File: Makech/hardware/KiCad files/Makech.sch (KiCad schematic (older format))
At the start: 45 parts, among them IC1 ULN2803, J1 USB_B_Micro, J2 SWD programmer, J3 ESP32-Exp, SW1 RST, U1 CONN_01X04, U2 ATSAMD21G18A-AU, U6 AP2114_3.3v, X1 Screw_Terminal_1x02

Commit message: Footprint complet
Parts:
- removed C2.1: 100nF, Capacitor_SMD:C_0603_1608Metric_Pad1.05x0.95mm_HandSolder, symbol Makech-rescue:C-RESCUE-Ogaki--Ogaki-rescue-Makech-rescue-Makech-rescue-Makech-r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
- removed R1, R3: 10K, Resistor_SMD:R_Array_Concave_2x0603, symbol Makech-rescue:R-SIL_8NB--Ogaki-rescue-Makech-rescue-Makech-rescue-Makech-rescue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
- removed R2: 10K, Resistors_SMD:R_0805_HandSoldering, symbol Makech-rescue:R-SIL_8NB--Ogaki-rescue-Makech-rescue-Makech-rescue-Makech-rescue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
- removed R4, R5: 1K, Resistors_ThroughHole:R_Array_SIP4, symbol Makech-rescue:R-SIL_8NB--Ogaki-rescue-Makech-rescue-Makech-rescue-Makech-rescue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
- removed S1, S2, S4, S5: switch, Button_Switch_THT:SW_PUSH-12mm_Wuerth-430476085716, symbol Makech-rescue:switch--Ogaki-rescue-Makech-rescue-Makech-rescue-Makech-rescue-Ma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
- removed S3: switch, Button_Switch_THT:SW_PUSH-12mm, symbol Makech-rescue:switch--Ogaki-rescue-Makech-rescue-Makech-rescue-Makech-rescue-Ma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
- removed S7: switch, Button_Switch_THT:SW_CuK_OS102011MA1QN1_SPDT_Angled, symbol Makech-rescue:switch--Ogaki-rescue-Makech-rescue-Makech-rescue-Makech-rescue-Ma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
- added R1, R2, R3, R4, R5, R6: 10K, Resistor_SMD:R_0805_2012Metric_Pad1.15x1.40mm_HandSolder, symbol Device:R_Small
- added R10, R11, R12, R9: 1K, Resistor_SMD:R_0805_2012Metric_Pad1.15x1.40mm_HandSolder, symbol Device:R_Small
- added S1, S2, S3, S4, S5: switch, Button_Switch_THT:SW_PUSH-12mm_Wuerth-430476085716, symbol Makech-rescue:SW_Push-Switch-Makech-rescue-Makech-rescue-Makech-rescue-Makech-r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
- added SW2: SW_DPDT_x2, Button_Switch_THT:SW_CuK_OS102011MA1QN1_SPDT_Angled, symbol Switch:SW_DPDT_x2
- SJ1: renamed from SJ2; footprint Connect:GS2 -> Jumper:SolderJumper-2_P1.3mm_Open_TrianglePad1.0x1.5mm
- X1: footprint Connect:bornier2 -> TerminalBlock:TerminalBlock_Altech_AK300-2_P5.00mm
- XH2: renamed from XH4; footprint Connector_Molex:Molex_KK-254_AE-6410-04A_1x04_P2.54mm_Vertical -> Connector_Molex:Molex_KK-254_AE-6410-05A_1x05_P2.54mm_Vertical
- renumbered C5 to C2, C6 to C3, C3 to C4, C4 to C5, C2 to C6, J2 to J1, J1 to J2, R6 to R7, R7 to R8, U2 to U1, U1 to U2, U6 to U3, XH3 to XH1
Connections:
- wire segments 280 -> 239
- no-connect marks 9 -> 10
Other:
- note removed: "Blue"

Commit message: Complete
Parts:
- J1: footprint Connector_PinHeader_1.00mm:PinHeader_2x02_P1.00mm_Vertical_SMD -> Connector_PinHeader_2.54mm:PinHeader_2x02_P2.54mm_Vertical_SMD
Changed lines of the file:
@@
 Text Label 7645 2390 0    60   ~ 0
 A3
-Text Label 5755 1260 1    60   ~ 0
-S1
-Text Label 6180 1260 1    60   ~ 0
-S2
-Text Label 6645 1260 1    60   ~ 0
-S3
-Text Label 7110 1255 1    60   ~ 0
-S5
-Text Label 7570 1270 1    60   ~ 0
-S4
 $Comp
 L Makech-rescue:JUMPER--Ogaki-rescue-Makech-rescue-Makech-rescue-Makech-rescue-Makech-rescue-Makech-rescue-Makech-rescue-Makech-rescue-Makech-rescue SJ1
@@
 F 0 "J1" H 1305 5897 50  0000 C CNN
 F 1 "SWD programmer" H 1305 5806 50  0000 C CNN
-F 2 "Connector_PinHeader_1.00mm:PinHeader_2x02_P1.00mm_Vertical_SMD" H 1255 5680 50  0001 C CNN
+F 2 "Connector_PinHeader_2.54mm:PinHeader_2x02_P2.54mm_Vertical_SMD" H 1255 5680 50  0001 C CNN
 F 3 "~" H 1255 5680 50  0001 C CNN
 	1    1255 5680

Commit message: USB correct
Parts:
- J2: footprint Connector_USB:USB_Micro-B_Amphenol_10103594-0001LF_Horizontal -> Connector_USB:USB_Micro-B_Wuerth_629105150521
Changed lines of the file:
@@
 F 0 "J2" H 2705 6257 50  0000 C CNN
 F 1 "USB_B_Micro" H 2705 6166 50  0000 C CNN
-F 2 "Connector_USB:USB_Micro-B_Amphenol_10103594-0001LF_Horizontal" H 2800 5740 50  0001 C CNN
+F 2 "Connector_USB:USB_Micro-B_Wuerth_629105150521" H 2800 5740 50  0001 C CNN
 F 3 "~" H 2800 5740 50  0001 C CNN
 F 4 "629105150521" H 2650 5790 50  0001 C CNN "manf#"

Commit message: change leds 3mm
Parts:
- J1: footprint Connector_PinHeader_2.54mm:PinHeader_2x02_P2.54mm_Vertical_SMD -> Pines:621X0421021
- LED1, LED2, LED3, LED4: footprint LED_SMD:LED_0805_2012Metric -> LEDs:LED_D3.0mm
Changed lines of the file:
@@
 F 0 "LED1" H 5755 3060 40  0000 C CNN
 F 1 "L" H 5755 2860 40  0001 C CNN
-F 2 "LED_SMD:LED_0805_2012Metric" H 5755 2960 60  0001 C CNN
+F 2 "LEDs:LED_D3.0mm" H 5755 2960 60  0001 C CNN
 F 3 "" H 5755 2960 60  0000 C CNN
 F 4 "APT2012LVBC/D" H 5755 2960 50  0001 C CNN "manf#"
@@
 F 0 "LED2" H 6385 3060 40  0000 C CNN
 F 1 "L" H 6385 2860 40  0001 C CNN
-F 2 "LED_SMD:LED_0805_2012Metric" H 6385 2960 60  0001 C CNN
+F 2 "LEDs:LED_D3.0mm" H 6385 2960 60  0001 C CNN
 F 3 "" H 6385 2960 60  0000 C CNN
 F 4 "APT2012SRCPRV" H 6385 2960 50  0001 C CNN "manf#"
@@
 F 0 "LED3" H 7015 3060 40  0000 C CNN
 F 1 "L" H 7015 2860 40  0001 C CNN
-F 2 "LED_SMD:LED_0805_2012Metric" H 7015 2960 60  0001 C CNN
+F 2 "LEDs:LED_D3.0mm" H 7015 2960 60  0001 C CNN
 F 3 "" H 7015 2960 60  0000 C CNN
 F 4 "APT2012SECK" H 7015 2960 50  0001 C CNN "manf#"
@@
 F 0 "LED4" H 7645 3060 40  0000 C CNN
 F 1 "L" H 7645 2860 40  0001 C CNN
-F 2 "LED_SMD:LED_0805_2012Metric" H 7645 2960 60  0001 C CNN
+F 2 "LEDs:LED_D3.0mm" H 7645 2960 60  0001 C CNN
 F 3 "" H 7645 2960 60  0000 C CNN
 F 4 "APT2012SGC" H 7645 2960 50  0001 C CNN "manf#"
@@
 F 0 "J1" H 1305 5897 50  0000 C CNN
 F 1 "SWD programmer" H 1305 5806 50  0000 C CNN
-F 2 "Connector_PinHeader_2.54mm:PinHeader_2x02_P2.54mm_Vertical_SMD" H 1255 5680 50  0001 C CNN
+F 2 "Pines:621X0421021" H 1255 5680 50  0001 C CNN
 F 3 "~" H 1255 5680 50  0001 C CNN
 	1    1255 5680

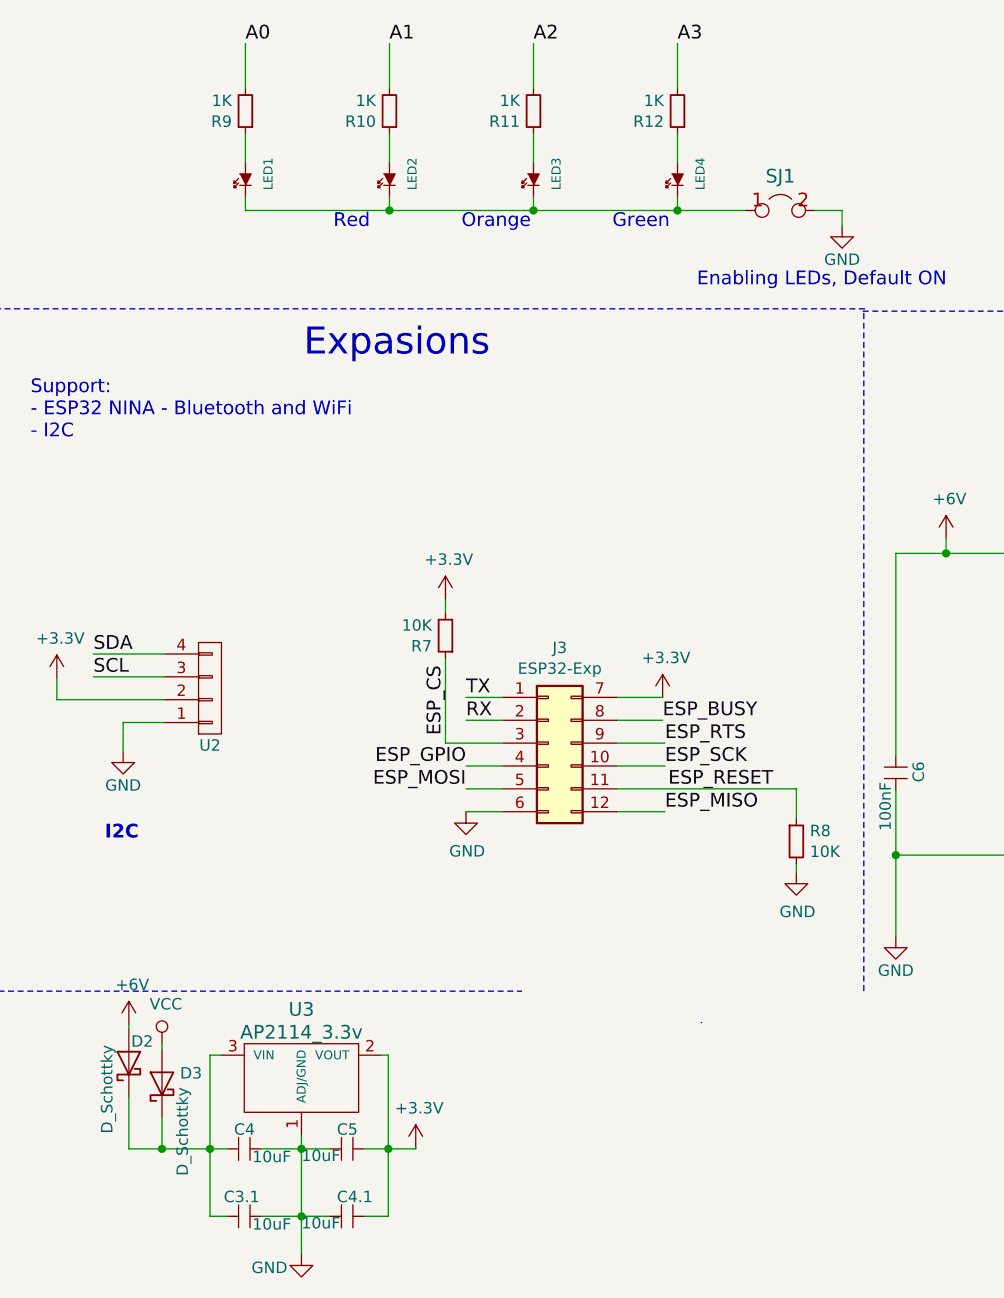
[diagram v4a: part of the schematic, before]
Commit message: remove jumper extra and capacitors
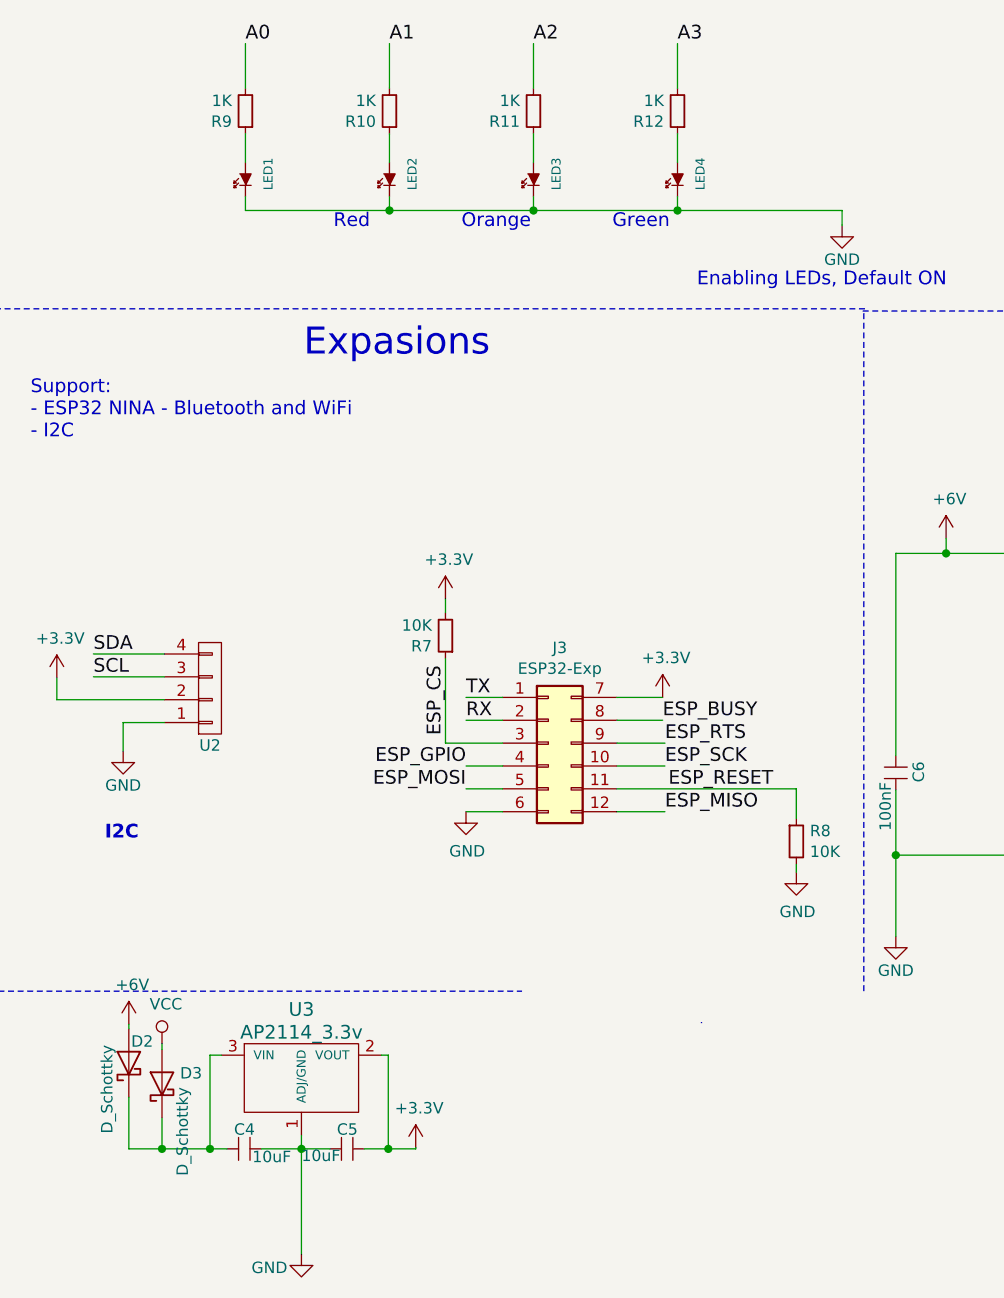
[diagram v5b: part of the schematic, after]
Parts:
- removed C3.1, C4.1: 10uF, Capacitor_SMD:C_0805_2012Metric_Pad1.15x1.40mm_HandSolder, symbol Makech-rescue:C-RESCUE-Ogaki--Ogaki-rescue-Makech-rescue-Makech-rescue-Makech-r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
- removed SJ1: JUMPER, Jumper:SolderJumper-2_P1.3mm_Open_TrianglePad1.0x1.5mm, symbol Makech-rescue:JUMPER--Ogaki-rescue-Makech-rescue-Makech-rescue-Makech-rescue-Ma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
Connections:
- net +3V3: now also C5.1, U3.2 (VOUT)
- net GND: now also LED1.1 (K), LED2.1 (K), LED3.1 (K), LED4.1 (K)
- net at C4.2, U3.3 (VIN): now also D2.1 (K), D3.1 (K)
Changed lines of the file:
@@
 A3
-$Comp
-L Makech-rescue:JUMPER--Ogaki-rescue-Makech-rescue-Makech-rescue-Makech-rescue-Makech-rescue-Makech-rescue-Makech-rescue-Makech-rescue-Makech-rescue SJ1
-U 1 1 58BAD83A
-P 8095 3120
-F 0 "SJ1" H 8095 3270 60  0000 C CNN
-F 1 "JUMPER" H 8095 3040 40  0001 C CNN
-F 2 "Jumper:SolderJumper-2_P1.3mm_Open_TrianglePad1.0x1.5mm" H 8095 3120 60  0001 C CNN
-F 3 "" H 8095 3120 60  0000 C CNN
-	1    8095 3120
-	1    0    0    -1
-$EndComp
 $Comp
 L Makech-rescue:GND--Ogaki-rescue-Makech-rescue-Makech-rescue-Makech-rescue-Makech-rescue-Makech-rescue-Makech-rescue-Makech-rescue-Makech-rescue #PWR026
@@
 	4190 495  4190 3360
 Wire Wire Line
-	8245 3120 8365 3120
-Wire Wire Line
 	8365 3120 8365 3185
 Wire Wire Line
@@
 	5600 6815 5650 6815
 Wire Wire Line
-	5675 7225 5600 7225
-Connection ~ 5600 7225
-Wire Wire Line
 	5825 7225 6000 7225
-Wire Wire Line
-	6275 7225 6380 7225
-Connection ~ 6380 7225
-$Comp
-L Makech-rescue:C-RESCUE-Ogaki--Ogaki-rescue-Makech-rescue-Makech-rescue-Makech-rescue-Makech-rescue-Makech-rescue-Makech-rescue-Makech-rescue-Makech-rescue C3.1
-U 1 1 58DE2448
-P 5775 7520
-F 0 "C3.1" V 5690 7405 50  0000 L CNN
-F 1 "10uF" V 5810 7530 50  0000 L CNN
-F 2 "Capacitor_SMD:C_0805_2012Metric_Pad1.15x1.40mm_HandSolder" H 5775 7520 60  0001 C CNN
-F 3 "" H 5775 7520 60  0000 C CNN
-F 4 "C0805X106K8RACAUTO" V 5775 7520 50  0001 C CNN "manf#"
-	1    5775 7520
-	0    1    1    0
-$EndComp
-$Comp
-L Makech-rescue:C-RESCUE-Ogaki--Ogaki-rescue-Makech-rescue-Makech-rescue-Makech-rescue-Makech-rescue-Makech-rescue-Makech-rescue-Makech-rescue-Makech-rescue C4.1
-U 1 1 58DE26E6
-P 6225 7520
-F 0 "C4.1" V 6140 7450 50  0000 L CNN
-F 1 "10uF" V 6255 7295 50  0000 L CNN
-F 2 "Capacitor_SMD:C_0805_2012Metric_Pad1.15x1.40mm_HandSolder" H 6225 7520 60  0001 C CNN
-F 3 "" H 6225 7520 60  0000 C CNN
-F 4 "C0805X106K8RACAUTO" V 6225 7520 50  0001 C CNN "manf#"
-	1    6225 7520
-	0    1    1    0
-$EndComp
-Wire Wire Line
-	5825 7520 6000 7520
-Wire Wire Line
-	5600 7520 5675 7520
-Wire Wire Line
-	6380 7520 6275 7520
-Wire Wire Line
-	6380 6815 6380 7225
-Wire Wire Line
-	5600 6815 5600 7225
 Wire Wire Line
 	6000 7165 6000 7225
 Connection ~ 6000 7225
-Connection ~ 6000 7520
-Wire Wire Line
-	7645 3120 7945 3120
 Wire Wire Line
 	6595 1920 6645 1920
@@
 	8820 4620 9880 4620
 Wire Wire Line
-	5600 7225 5600 7520
-Wire Wire Line
-	6380 7225 6380 7520
-Wire Wire Line
 	6000 7225 6125 7225
-Wire Wire Line
-	6000 7225 6000 7520
-Wire Wire Line
-	6000 7520 6125 7520
-Wire Wire Line
-	6000 7520 6000 7685
 Wire Notes Line
 	8460 6535 8460 3555
@@
 	1    0    0    -1
 $EndComp
-Wire Wire Line
-	6385 7225 6500 7225
-Wire Wire Line
-	6500 7225 6500 7220
 $Comp
 L Makech-rescue:+3.3V-power-Makech-rescue-Makech-rescue-Makech-rescue-Makech-rescue-Makech-rescue-Makech-rescue-Makech-rescue #PWR020
@@
 	2725 6530 2720 6530
 Wire Wire Line
-	5595 7225 5390 7225
-Wire Wire Line
 	5390 7225 5390 7090
-Connection ~ 5390 7225
 $Comp
 L Makech-rescue:VCC-power-Makech-rescue-Makech-rescue-Makech-rescue-Makech-rescue-Makech-rescue-Makech-rescue-Makech-rescue #PWR018
@@
 Wire Wire Line
 	7110 1920 7570 1920
+Wire Wire Line
+	7645 3120 8365 3120
+Wire Wire Line
+	6000 7225 6000 7685
+Wire Wire Line
+	6275 7225 6380 7225
+Wire Wire Line
+	6500 7225 6500 7220
+Wire Wire Line
+	6380 6815 6380 7225
+Connection ~ 6380 7225
+Wire Wire Line
+	6380 7225 6500 7225
+Wire Wire Line
+	5390 7225 5390 7220
+Wire Wire Line
+	5390 7225 5600 7225
+Connection ~ 5390 7225
+Wire Wire Line
+	5600 6815 5600 7225
+Connection ~ 5600 7225
+Wire Wire Line
+	5600 7225 5675 7225
 $EndSCHEMATC

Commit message: Fix source motors
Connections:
- net RAW is gone; now on net +6V: XH1.1 (P1), XH2.1 (P1)
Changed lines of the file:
@@
 Text Label 9330 5555 0    60   ~ 0
 D4
-Text Label 10695 5905 0    60   ~ 0
-RAW
-Text Label 10695 5010 0    60   ~ 0
-RAW
 Text Label 10700 4610 0    60   ~ 0
 ML1
@@
 	4545 1240 4885 1240
 Wire Wire Line
-	4885 920  4990 920
-Wire Wire Line
 	4885 980  4885 920
 Wire Notes Line
@@
 Wire Wire Line
 	1420 1305 1290 1305
-Wire Wire Line
-	4990 920  4990 855
 $Comp
 L Makech-rescue:+3.3V-power-Makech-rescue-Makech-rescue-Makech-rescue-Makech-rescue-Makech-rescue-Makech-rescue-Makech-rescue #PWR015
 U 1 1 5D10D595
-P 4990 855
-F 0 "#PWR015" H 4990 705 50  0001 C CNN
-F 1 "+3.3V" H 5005 1028 50  0000 C CNN
-F 2 "" H 4990 855 50  0001 C CNN
-F 3 "" H 4990 855 50  0001 C CNN
-	1    4990 855
+P 4885 920
+F 0 "#PWR015" H 4885 770 50  0001 C CNN
+F 1 "+3.3V" H 4900 1093 50  0000 C CNN
+F 2 "" H 4885 920 50  0001 C CNN
+F 3 "" H 4885 920 50  0001 C CNN
+	1    4885 920
 	1    0    0    -1
 $EndComp
@@
 Wire Wire Line
 	5600 7225 5675 7225
+$Comp
+L power:+6V #PWR0101
+U 1 1 5CA32BB8
+P 10515 6030
+F 0 "#PWR0101" H 10515 5880 50  0001 C CNN
+F 1 "+6V" H 10530 6203 50  0000 C CNN
+F 2 "" H 10515 6030 50  0001 C CNN
+F 3 "" H 10515 6030 50  0001 C CNN
+	1    10515 6030
+	1    0    0    -1
+$EndComp
+$Comp
+L power:+6V #PWR0102
+U 1 1 5CA32C6B
+P 10590 5160
+F 0 "#PWR0102" H 10590 5010 50  0001 C CNN
+F 1 "+6V" H 10605 5333 50  0000 C CNN
+F 2 "" H 10590 5160 50  0001 C CNN
+F 3 "" H 10590 5160 50  0001 C CNN
+	1    10590 5160
+	1    0    0    -1
+$EndComp
+Wire Wire Line
+	10695 5010 10695 5210
+Wire Wire Line
+	10695 5210 10590 5210
+Wire Wire Line
+	10590 5210 10590 5160
+Wire Wire Line
+	10695 5905 10695 6030
+Wire Wire Line
+	10695 6030 10515 6030
 $EndSCHEMATC

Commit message: add symbol jumper
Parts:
- removed JP1: CONN_01X02, Connector_Wire:SolderWirePad_1x02_P3.81mm_Drill0.8mm, symbol Makech-rescue:CONN_01X02--Ogaki-rescue-Makech-rescue-Makech-rescue-Makech-rescu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
- added JP1: Jumper, symbol Jumper:SolderJumper_2_Bridged
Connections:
- net D11: now also JP1.1 (A)
- net at Z1.1: now also JP1.2 (B)
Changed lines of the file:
@@
 Text Notes 7730 3460 0    60   ~ 0
 Enabling LEDs, Default ON\n
-$Comp
-L Makech-rescue:CONN_01X02--Ogaki-rescue-Makech-rescue-Makech-rescue-Makech-rescue-Makech-rescue-Makech-rescue-Makech-rescue-Makech-rescue-Makech-rescue JP1
-U 1 1 58BAEF93
-P 4300 5565
-F 0 "JP1" H 4300 5715 50  0000 C CNN
-F 1 "CONN_01X02" V 4400 5565 50  0001 C CNN
-F 2 "Connector_Wire:SolderWirePad_1x02_P3.81mm_Drill0.8mm" H 4300 5565 50  0001 C CNN
-F 3 "" H 4300 5565 50  0000 C CNN
-F 4 "61300211121" H 4300 5565 50  0001 C CNN "manf#"
-	1    4300 5565
-	1    0    0    -1
-$EndComp
 Text Notes 4445 5095 2    118  ~ 0
 BUZZ
@@
 	1    0    0    -1
 $EndComp
-Text Label 3880 5515 0    60   ~ 0
+Text Label 4025 5260 2    60   ~ 0
 D11
 $Comp
@@
 Wire Wire Line
 	8365 3120 8365 3185
-Wire Wire Line
-	4100 5515 3880 5515
 Wire Wire Line
 	4115 5910 4075 5910
@@
 Wire Wire Line
 	10695 6030 10515 6030
+$Comp
+L Jumper:SolderJumper_2_Bridged JP1
+U 1 1 5CA75BE5
+P 4100 5465
+F 0 "JP1" V 4054 5533 50  0000 L CNN
+F 1 "Jumper" H 3980 5380 50  0000 L CNN
+F 2 "" H 4100 5465 50  0001 C CNN
+F 3 "~" H 4100 5465 50  0001 C CNN
+	1    4100 5465
+	0    1    1    0
+$EndComp
+Wire Wire Line
+	4100 5315 4100 5260
+Wire Wire Line
+	4100 5260 4025 5260
 $EndSCHEMATC

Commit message: update labels
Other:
- note added: "ESP32"
- note added: "SOURCE"
- note removed: "Enabling LEDs, Default ON\n"
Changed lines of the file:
@@
 	-1   0    0    -1
 $EndComp
-Text Notes 7730 3460 0    60   ~ 0
-Enabling LEDs, Default ON\n
 Text Notes 4445 5095 2    118  ~ 0
 BUZZ
@@
 Wire Wire Line
 	4100 5260 4025 5260
+Text Notes 6995 5975 0    60   ~ 12
+ESP32
+Text Notes 2570 6715 0    118  ~ 0
+SOURCE
 $EndSCHEMATC
